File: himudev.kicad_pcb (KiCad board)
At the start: 4 copper layers, 93.6 x 43.6 mm, 136 parts, among them J1 USB-C-16PIN, J2 M20-8770642R, J3 M20-8770642R, J4 20021121-00010C4LF, J5 M20-8762042, Q1 IRLML6402, Q2 BSS214NW, Q3 BSS214NW, Q4 BSS214NW, Q5 BSS214NW, Q6 BSS214NW, U1 FT230XS, U2 MCP1726-3302ESN, U3 MIC5319-1.8YD5-TR, U4 IS25WP032D, U5 FE310-G002, U6 ICM-20948, U7 BMP388, X1 KX2132709Z, Y1 TSX-3225 16.0000MF18X-AC0

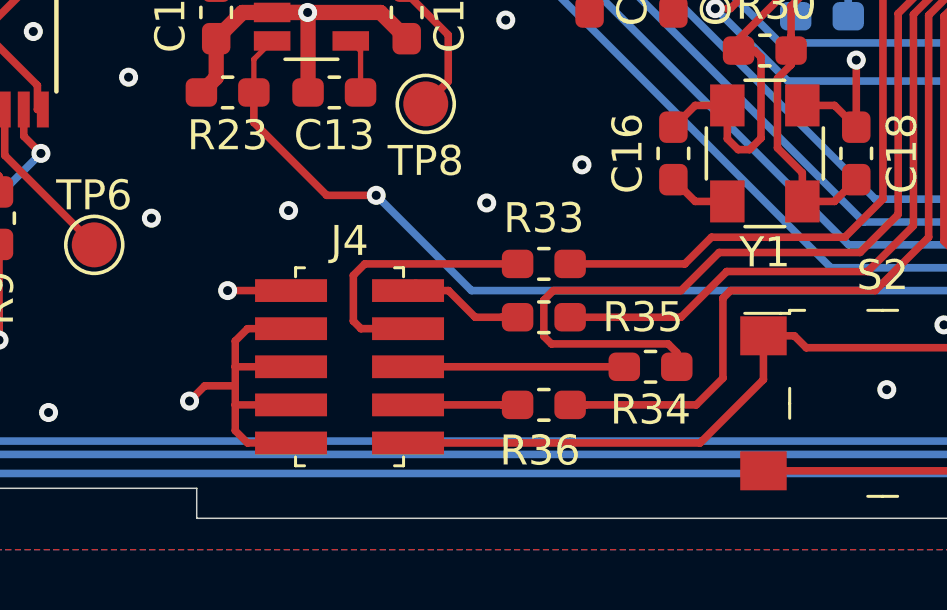
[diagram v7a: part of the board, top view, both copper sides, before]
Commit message: Move J4 up by 1 mm, add copper keepout around GND pins
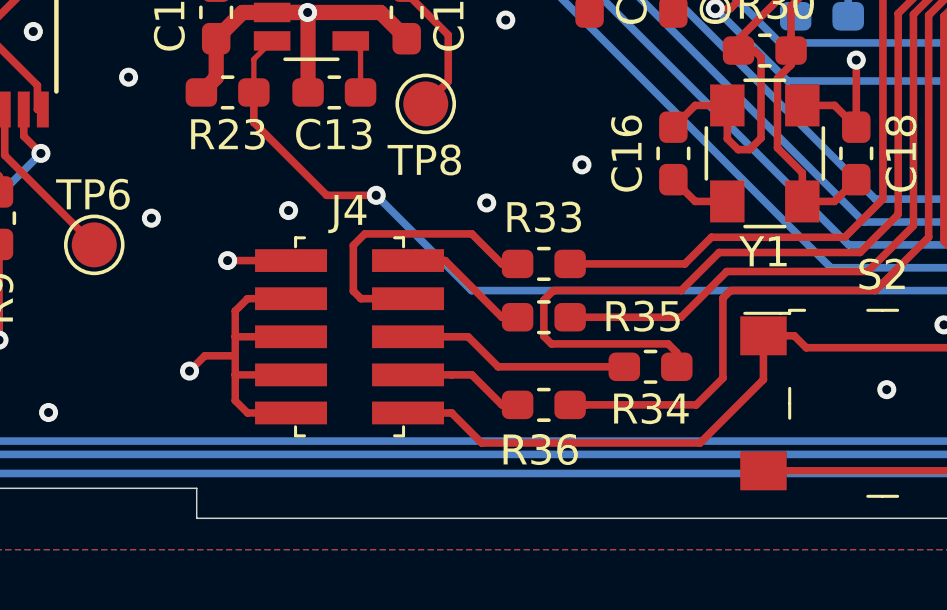
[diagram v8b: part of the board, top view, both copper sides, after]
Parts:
- moved J4 1.00 mm to (142.5, 117.4)
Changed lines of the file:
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@@
     (thickness 1.6)
     (drawings 49)
-    (tracks 1381)
+    (tracks 1388)
     (zones 0)
     (modules 136)
@@
   )
   (setup
-    (last_trace_width 0.508)
+    (last_trace_width 0.254)
     (user_trace_width 0.127)
     (user_trace_width 0.1778)
@@
   )
   (module digikey-footprints:PinHeader_2x5_P1.27mm (layer F.Cu)
-    (at 142.494 118.364 270)
+    (at 142.494 117.364 270)
     (descr https://cdn.amphenol-icc.com/media/wysiwyg/files/drawing/20021121.pdf)
     (attr smd)
@@
   (via (at 118.11 108.966) (size 0.635) (drill 0.3) (layers F.Cu B.Cu) (net 1))
   (via (at 113.792 105.283) (size 0.635) (drill 0.3) (layers F.Cu B.Cu) (net 1))
-  (segment (start 138.684 120.494) (end 139.094 120.904) (width 0.25) (layer F.Cu) (net 1))
-  (segment (start 139.094 117.094) (end 138.684 117.504) (width 0.25) (layer F.Cu) (net 1))
-  (segment (start 139.094 120.904) (end 140.544 120.904) (width 0.25) (layer F.Cu) (net 1))
-  (segment (start 140.544 117.094) (end 139.094 117.094) (width 0.25) (layer F.Cu) (net 1))
-  (segment (start 140.544 118.364) (end 138.684 118.364) (width 0.25) (layer F.Cu) (net 1))
-  (segment (start 138.684 117.504) (end 138.684 118.364) (width 0.25) (layer F.Cu) (net 1))
-  (segment (start 140.544 119.634) (end 138.684 119.634) (width 0.25) (layer F.Cu) (net 1))
-  (segment (start 138.684 119.634) (end 138.684 120.494) (width 0.25) (layer F.Cu) (net 1))
+  (segment (start 138.684 119.494) (end 139.094 119.904) (width 0.25) (layer F.Cu) (net 1))
+  (segment (start 139.094 116.094) (end 138.684 116.504) (width 0.25) (layer F.Cu) (net 1))
+  (segment (start 139.094 119.904) (end 140.544 119.904) (width 0.25) (layer F.Cu) (net 1))
+  (segment (start 140.544 116.094) (end 139.094 116.094) (width 0.25) (layer F.Cu) (net 1))
+  (segment (start 140.544 117.364) (end 138.684 117.364) (width 0.25) (layer F.Cu) (net 1))
+  (segment (start 138.684 116.504) (end 138.684 117.364) (width 0.25) (layer F.Cu) (net 1))
+  (segment (start 140.544 118.634) (end 138.684 118.634) (width 0.25) (layer F.Cu) (net 1))
+  (segment (start 138.684 118.634) (end 138.684 119.494) (width 0.25) (layer F.Cu) (net 1))
   (segment (start 118.119 95.885) (end 118.119 98.171) (width 0.254) (layer F.Cu) (net 1))
   (segment (start 118.119 105.029) (end 118.119 107.315) (width 0.254) (layer F.Cu) (net 1))
@@
   (segment (start 141.097 106.553) (end 139.914 106.553) (width 0.508) (layer F.Cu) (net 1))
   (via (at 141.097 106.553) (size 0.635) (drill 0.3) (layers F.Cu B.Cu) (net 1))
-  (via (at 137.16 119.507) (size 0.635) (drill 0.3) (layers F.Cu B.Cu) (net 1))
-  (segment (start 137.668 118.999) (end 137.16 119.507) (width 0.254) (layer F.Cu) (net 1))
-  (segment (start 138.684 118.999) (end 137.668 118.999) (width 0.254) (layer F.Cu) (net 1))
-  (segment (start 138.684 118.999) (end 138.684 119.634) (width 0.25) (layer F.Cu) (net 1))
-  (segment (start 138.684 118.364) (end 138.684 118.999) (width 0.25) (layer F.Cu) (net 1))
+  (via (at 137.16 118.507) (size 0.635) (drill 0.3) (layers F.Cu B.Cu) (net 1))
+  (segment (start 137.668 117.999) (end 137.16 118.507) (width 0.254) (layer F.Cu) (net 1))
+  (segment (start 138.684 117.999) (end 137.668 117.999) (width 0.254) (layer F.Cu) (net 1))
+  (segment (start 138.684 117.999) (end 138.684 118.634) (width 0.25) (layer F.Cu) (net 1))
+  (segment (start 138.684 117.364) (end 138.684 117.999) (width 0.25) (layer F.Cu) (net 1))
   (via (at 184.404 97.79) (size 0.635) (drill 0.3) (layers F.Cu B.Cu) (net 1))
   (segment (start 182.133 97.79) (end 184.404 97.79) (width 0.762) (layer F.Cu) (net 1))
@@
   (segment (start 139.914 105.603) (end 141.031 105.603) (width 0.508) (layer F.Cu) (net 7))
   (segment (start 141.031 105.603) (end 141.224 105.41) (width 0.508) (layer F.Cu) (net 7))
-  (via (at 138.43 115.824) (size 0.635) (drill 0.3) (layers F.Cu B.Cu) (net 7))
-  (segment (start 140.544 115.824) (end 138.43 115.824) (width 0.254) (layer F.Cu) (net 7))
+  (via (at 138.43 114.824) (size 0.635) (drill 0.3) (layers F.Cu B.Cu) (net 7))
+  (segment (start 140.544 114.824) (end 138.43 114.824) (width 0.254) (layer F.Cu) (net 7))
   (via (at 167.005 105.791) (size 0.635) (drill 0.3) (layers F.Cu B.Cu) (net 7))
   (segment (start 166.162064 105.41) (end 166.543238 105.41) (width 0.254) (layer F.Cu) (net 7))
@@
   (segment (start 127.635 121.158) (end 125.809 119.332) (width 0.254) (layer F.Cu) (net 26))
   (segment (start 125.809 119.332) (end 125.809 118.236) (width 0.254) (layer F.Cu) (net 26))
-  (segment (start 156.291 118.791) (end 156.291 117.332) (width 0.254) (layer F.Cu) (net 27))
-  (segment (start 154.178 120.904) (end 144.444 120.904) (width 0.254) (layer F.Cu) (net 27))
-  (segment (start 156.291 118.791) (end 154.178 120.904) (width 0.254) (layer F.Cu) (net 27))
   (segment (start 169.164 120.269) (end 166.257 120.269) (width 0.254) (layer F.Cu) (net 27))
   (segment (start 166.257 120.269) (end 166.243 120.283) (width 0.254) (layer F.Cu) (net 27))
@@
   (segment (start 164.241 117.332) (end 163.212 117.332) (width 0.254) (layer F.Cu) (net 27))
   (segment (start 163.212 117.332) (end 162.815 117.729) (width 0.254) (layer F.Cu) (net 27))
+  (segment (start 145.898 119.904) (end 144.444 119.904) (width 0.254) (layer F.Cu) (net 27))
+  (segment (start 146.898 120.904) (end 145.898 119.904) (width 0.254) (layer F.Cu) (net 27))
+  (segment (start 154.178 120.904) (end 146.898 120.904) (width 0.254) (layer F.Cu) (net 27))
+  (segment (start 156.291 117.332) (end 156.291 118.791) (width 0.254) (layer F.Cu) (net 27))
+  (segment (start 156.291 118.791) (end 154.178 120.904) (width 0.254) (layer F.Cu) (net 27))
   (segment (start 164.973 88.919) (end 164.973 86.868) (width 0.254) (layer B.Cu) (net 28))
   (segment (start 162.927 91.44) (end 162.927 90.965) (width 0.254) (layer B.Cu) (net 28))
@@
   (segment (start 176.149 90.941) (end 177.165 89.925) (width 0.254) (layer F.Cu) (net 35))
   (segment (start 176.149 91.186) (end 176.149 90.941) (width 0.254) (layer F.Cu) (net 35))
+  (segment (start 145.898 118.634) (end 144.444 118.634) (width 0.254) (layer F.Cu) (net 37))
+  (segment (start 146.571 118.634) (end 145.898 118.634) (width 0.254) (layer F.Cu) (net 37))
+  (segment (start 147.571 119.634) (end 146.571 118.634) (width 0.254) (layer F.Cu) (net 37))
   (segment (start 148.096 119.634) (end 147.571 119.634) (width 0.254) (layer F.Cu) (net 37))
-  (segment (start 148.096 119.634) (end 144.444 119.634) (width 0.254) (layer F.Cu) (net 37))
-  (segment (start 151.652 118.364) (end 144.444 118.364) (width 0.254) (layer F.Cu) (net 38))
-  (segment (start 142.875 117.094) (end 144.444 117.094) (width 0.254) (layer F.Cu) (net 39))
-  (segment (start 142.621 116.84) (end 142.875 117.094) (width 0.254) (layer F.Cu) (net 39))
-  (segment (start 142.621 115.316) (end 142.621 116.84) (width 0.254) (layer F.Cu) (net 39))
-  (segment (start 143.002 114.935) (end 142.621 115.316) (width 0.254) (layer F.Cu) (net 39))
-  (segment (start 148.096 114.935) (end 143.002 114.935) (width 0.254) (layer F.Cu) (net 39))
-  (segment (start 144.698 115.57) (end 144.444 115.824) (width 0.254) (layer F.Cu) (net 40))
-  (segment (start 145.793 115.824) (end 144.444 115.824) (width 0.254) (layer F.Cu) (net 40))
+  (segment (start 146.447 117.364) (end 144.444 117.364) (width 0.254) (layer F.Cu) (net 38))
+  (segment (start 151.652 118.364) (end 147.447 118.364) (width 0.254) (layer F.Cu) (net 38))
+  (segment (start 147.447 118.364) (end 146.447 117.364) (width 0.254) (layer F.Cu) (net 38))
+  (segment (start 142.875 116.094) (end 144.444 116.094) (width 0.254) (layer F.Cu) (net 39))
+  (segment (start 142.621 115.84) (end 142.875 116.094) (width 0.254) (layer F.Cu) (net 39))
+  (segment (start 142.621 114.316) (end 142.621 115.84) (width 0.254) (layer F.Cu) (net 39))
+  (segment (start 143.002 113.935) (end 142.621 114.316) (width 0.254) (layer F.Cu) (net 39))
+  (segment (start 146.571 113.935) (end 143.002 113.935) (width 0.254) (layer F.Cu) (net 39))
+  (segment (start 147.571 114.935) (end 146.571 113.935) (width 0.254) (layer F.Cu) (net 39))
+  (segment (start 148.096 114.935) (end 147.571 114.935) (width 0.254) (layer F.Cu) (net 39))
+  (segment (start 144.698 114.57) (end 144.444 114.824) (width 0.254) (layer F.Cu) (net 40))
+  (segment (start 145.682 114.824) (end 144.444 114.824) (width 0.254) (layer F.Cu) (net 40))
+  (segment (start 147.571 116.713) (end 145.682 114.824) (width 0.254) (layer F.Cu) (net 40))
   (segment (start 148.096 116.713) (end 147.571 116.713) (width 0.254) (layer F.Cu) (net 40))
-  (segment (start 146.682 116.713) (end 145.793 115.824) (width 0.254) (layer F.Cu) (net 40))
-  (segment (start 148.096 116.713) (end 146.682 116.713) (width 0.254) (layer F.Cu) (net 40))
   (segment (start 171.704 108.597) (end 171.704 109.601) (width 0.254) (layer F.Cu) (net 41))
   (segment (start 166.907 103.8) (end 171.704 108.597) (width 0.254) (layer F.Cu) (net 41))
@@
       )
     )
+  )
+  (zone (net 0) (net_name "") (layer F.Cu) (hatch edge 0.508)
+    (connect_pads (clearance 0.381))
+    (min_thickness 0.254)
+    (keepout (tracks allowed) (vias allowed) (copperpour not_allowed))
+    (fill (arc_segments 32) (thermal_gap 0.508) (thermal_bridge_width 0.508))
+    (polygon
+      (pts
+        (xy 142.24 120.777) (xy 138.43 120.777) (xy 138.43 115.57) (xy 142.24 115.57)
+      )
+    )
